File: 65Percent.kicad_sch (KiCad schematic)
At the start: 22 parts, among them J1 ISP Headers, J2 USB C Port, SW1 Reset SW, U1 ATmega32A-A, Y1 16MHz

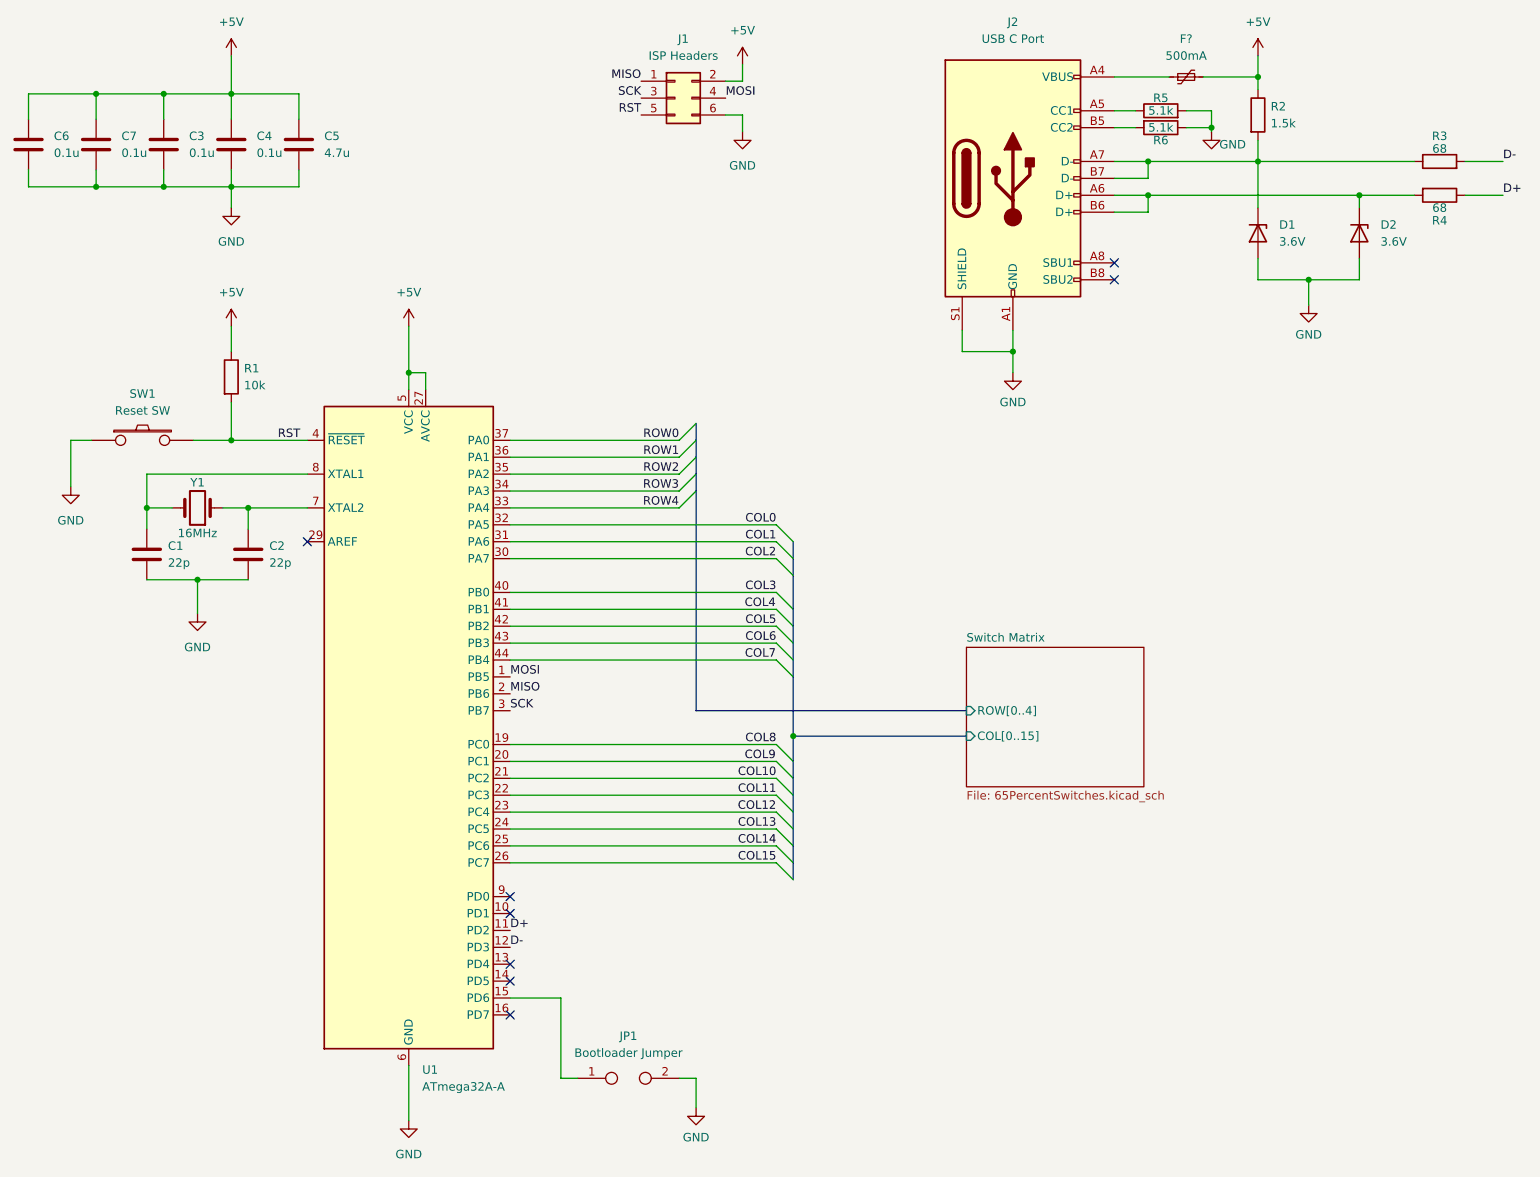
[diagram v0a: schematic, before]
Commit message: Added fuses, column and diode wirings
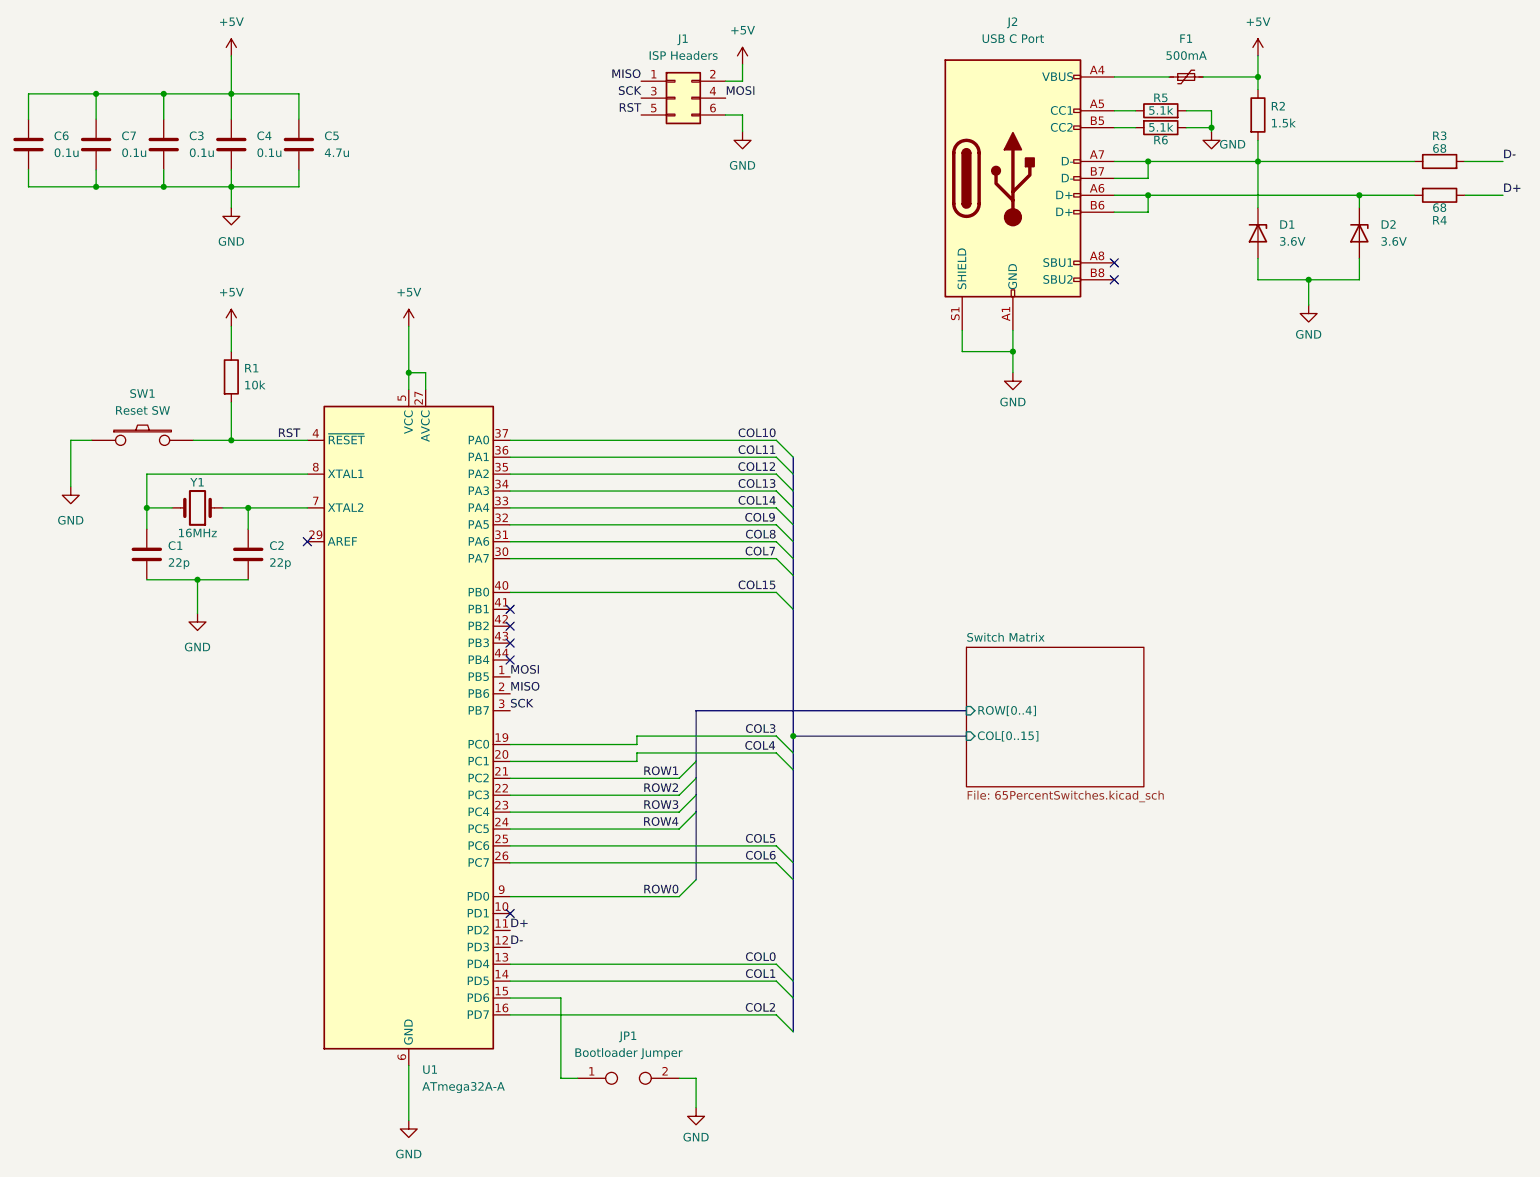
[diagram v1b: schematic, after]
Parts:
- F1: renamed from F?; footprint (none) -> Fuse:Fuse_0805_2012Metric_Pad1.15x1.40mm_HandSolder
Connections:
- net COL0: now also U1.13 (PD4); no longer U1.32 (PA5)
- net COL1: now also U1.14 (PD5); no longer U1.31 (PA6)
- net COL10: now also U1.37 (PA0); no longer U1.21 (PC2)
- net COL11: now also U1.36 (PA1); no longer U1.22 (PC3)
- net COL12: now also U1.35 (PA2); no longer U1.23 (PC4)
- net COL13: now also U1.34 (PA3); no longer U1.24 (PC5)
- net COL14: now also U1.33 (PA4); no longer U1.25 (PC6)
- net COL15: now also U1.40 (PB0); no longer U1.26 (PC7)
- net COL2: now also U1.16 (PD7); no longer U1.30 (PA7)
- net COL3: now also U1.19 (PC0); no longer U1.40 (PB0)
- net COL4: now also U1.20 (PC1); no longer U1.41 (PB1)
- net COL5: now also U1.25 (PC6); no longer U1.42 (PB2)
- net COL6: now also U1.26 (PC7); no longer U1.43 (PB3)
- net COL7: now also U1.30 (PA7); no longer U1.44 (PB4)
- net COL8: now also U1.31 (PA6); no longer U1.19 (PC0)
- net COL9: now also U1.32 (PA5); no longer U1.20 (PC1)
- net ROW0: now also U1.9 (PD0); no longer U1.37 (PA0)
- net ROW1: now also U1.21 (PC2); no longer U1.36 (PA1)
- net ROW2: now also U1.22 (PC3); no longer U1.35 (PA2)
- net ROW3: now also U1.23 (PC4); no longer U1.34 (PA3)
- net ROW4: now also U1.24 (PC5); no longer U1.33 (PA4)

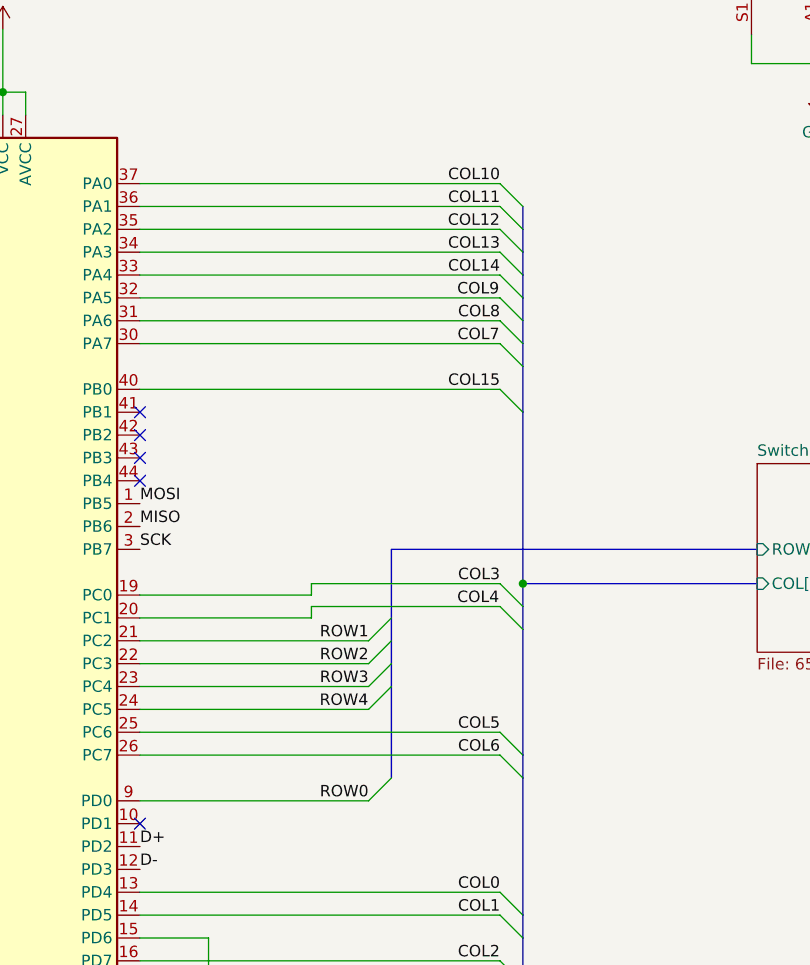
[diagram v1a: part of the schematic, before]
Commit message: Completed first pass at v1 board
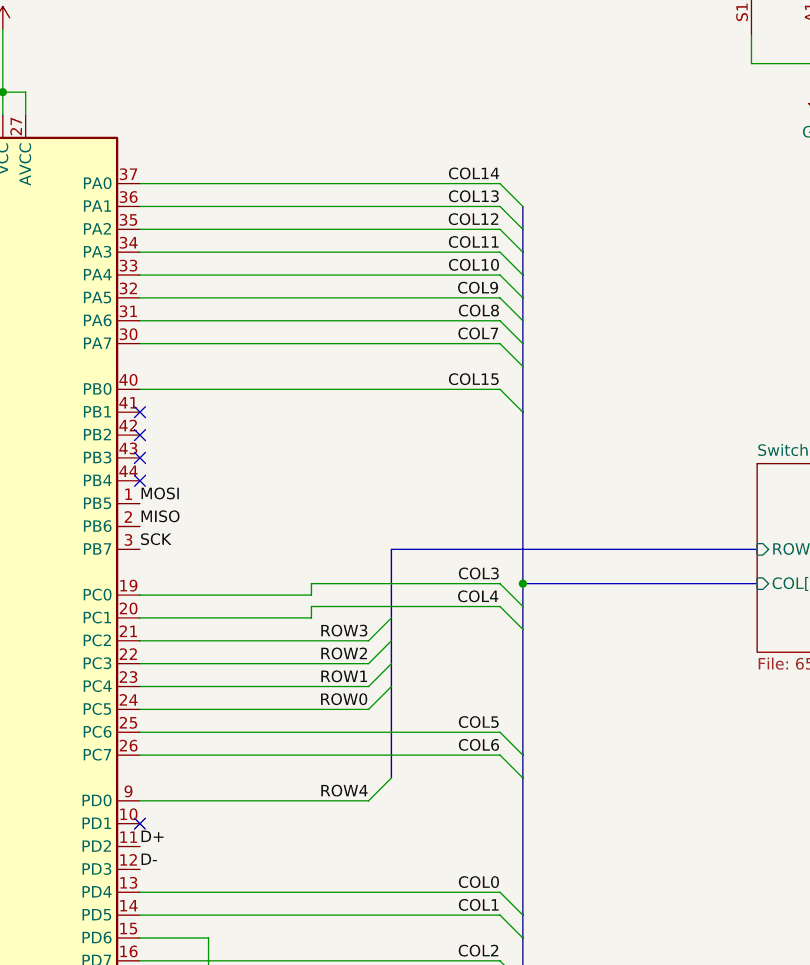
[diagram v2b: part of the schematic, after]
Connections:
- net COL10: now also U1.33 (PA4); no longer U1.37 (PA0)
- net COL11: now also U1.34 (PA3); no longer U1.36 (PA1)
- net COL13: now also U1.36 (PA1); no longer U1.34 (PA3)
- net COL14: now also U1.37 (PA0); no longer U1.33 (PA4)
- net ROW0: now also U1.24 (PC5); no longer U1.9 (PD0)
- net ROW1: now also U1.23 (PC4); no longer U1.21 (PC2)
- net ROW3: now also U1.21 (PC2); no longer U1.23 (PC4)
- net ROW4: now also U1.9 (PD0); no longer U1.24 (PC5)
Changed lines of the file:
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@@
     (effects (font (size 1.27 1.27)) (justify left bottom))
   )
-  (label "COL13" (at 128.905 85.725 180)
+  (label "COL11" (at 128.905 85.725 180)
     (effects (font (size 1.27 1.27)) (justify right bottom))
   )
@@
     (effects (font (size 1.27 1.27)) (justify right bottom))
   )
-  (label "ROW4" (at 114.2671 136.525 180)
+  (label "ROW0" (at 114.2671 136.525 180)
     (effects (font (size 1.27 1.27)) (justify right bottom))
   )
@@
     (effects (font (size 1.27 1.27)) (justify right bottom))
   )
-  (label "ROW0" (at 114.3 146.685 180)
+  (label "ROW4" (at 114.3 146.685 180)
     (effects (font (size 1.27 1.27)) (justify right bottom))
   )
-  (label "COL11" (at 128.905 80.645 180)
+  (label "COL13" (at 128.905 80.645 180)
     (effects (font (size 1.27 1.27)) (justify right bottom))
   )
@@
     (effects (font (size 1.27 1.27)) (justify right bottom))
   )
-  (label "COL10" (at 128.905 78.105 180)
+  (label "COL14" (at 128.905 78.105 180)
     (effects (font (size 1.27 1.27)) (justify right bottom))
   )
-  (label "ROW1" (at 114.3 128.905 180)
+  (label "ROW3" (at 114.3 128.905 180)
     (effects (font (size 1.27 1.27)) (justify right bottom))
   )
@@
     (effects (font (size 1.27 1.27)) (justify right bottom))
   )
-  (label "COL14" (at 128.905 88.265 180)
+  (label "COL10" (at 128.905 88.265 180)
     (effects (font (size 1.27 1.27)) (justify right bottom))
   )
@@
     (effects (font (size 1.27 1.27)) (justify right bottom))
   )
-  (label "ROW3" (at 114.3 133.985 180)
+  (label "ROW1" (at 114.3 133.985 180)
     (effects (font (size 1.27 1.27)) (justify right bottom))
   )

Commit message: Add pdfs of schematic and pcb
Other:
- title: (none) -> AndyBoard
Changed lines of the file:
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@@
 (kicad_sch (version 20211123) (generator eeschema)
   (paper "A4")
+  (title_block
+    (title "AndyBoard")
+    (date "2023-08-29")
+    (rev "1")
+  )
   (junction (at 164.465 64.77) (diameter 0) (color 0 0 0 0)
   )
